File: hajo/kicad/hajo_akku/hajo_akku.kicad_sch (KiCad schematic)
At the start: 21 parts, among them J1 Seetalk NG, J2 Debug, J3 Batteries, U1 MCP2562, U2 LF50CV, U3 WeMos_S2_mini

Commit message: pcv rework
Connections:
- net DebugRX: now also J2.3 (Pin_3), U3.32 (GPIO40); no longer J2.4 (Pin_4), U3.15 (GPIO37)
- net DebugTX: now also J2.4 (Pin_4); no longer J2.3 (Pin_3)
- net GND: now also U1.8 (STBY), U3.17 (GPIO1); no longer U3.22 (GPIO10)
- net STBY: no longer names the net of U3.29 (GPIO34)
- net STBY: no longer U1.8 (STBY)
- no-connect marks 18 -> 21
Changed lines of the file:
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@@
   (junction (at 25.4 73.66) (diameter 0) (color 0 0 0 0)
   )
+  (junction (at 49.53 48.26) (diameter 0) (color 0 0 0 0)
+  )
   (junction (at 40.64 86.36) (diameter 0) (color 0 0 0 0)
   )
@@
   (junction (at 140.97 29.21) (diameter 0) (color 0 0 0 0)
   )
-  (no_connect (at 195.58 44.45))
   (no_connect (at 165.1 69.85))
   (no_connect (at 195.58 69.85))
   (no_connect (at 195.58 77.47))
+  (no_connect (at 165.1 64.77))
   (no_connect (at 195.58 52.07))
-  (no_connect (at 165.1 80.01))
+  (no_connect (at 165.1 72.39))
   (no_connect (at 165.1 54.61))
+  (no_connect (at 195.58 67.31))
   (no_connect (at 195.58 46.99))
   (no_connect (at 195.58 74.93))
@@
   (no_connect (at 165.1 39.37))
   (no_connect (at 195.58 62.23))
+  (no_connect (at 165.1 44.45))
+  (no_connect (at 165.1 46.99))
   (no_connect (at 195.58 57.15))
   (no_connect (at 195.58 64.77))
@@
     (stroke (width 0) (type default))
   )
-  (wire (pts (xy 49.53 46.99) (xy 49.53 49.53))
+  (wire (pts (xy 49.53 46.99) (xy 49.53 48.26))
     (stroke (width 0) (type default))
   )
@@
     (stroke (width 0) (type default))
   )
-  (wire (pts (xy 157.48 64.77) (xy 165.1 64.77))
-    (stroke (width 0) (type default))
-  )
   (wire (pts (xy 82.55 86.36) (xy 85.09 86.36))
     (stroke (width 0) (type default))
@@
     (stroke (width 0) (type default))
   )
+  (wire (pts (xy 49.53 48.26) (xy 49.53 50.8))
+    (stroke (width 0) (type default))
+  )
   (wire (pts (xy 154.94 77.47) (xy 165.1 77.47))
     (stroke (width 0) (type default))
@@
     (stroke (width 0) (type default))
   )
-  (wire (pts (xy 31.75 41.91) (xy 36.83 41.91))
+  (wire (pts (xy 34.29 48.26) (xy 49.53 48.26))
     (stroke (width 0) (type default))
   )
@@
     (stroke (width 0) (type default))
   )
-  (wire (pts (xy 154.94 72.39) (xy 165.1 72.39))
+  (wire (pts (xy 154.94 80.01) (xy 165.1 80.01))
     (stroke (width 0) (type default))
   )
@@
     (stroke (width 0) (type default))
   )
+  (wire (pts (xy 36.83 41.91) (xy 34.29 41.91))
+    (stroke (width 0) (type default))
+  )
   (wire (pts (xy 134.62 48.26) (xy 140.97 48.26))
     (stroke (width 0) (type default))
@@
     (stroke (width 0) (type default))
   )
+  (wire (pts (xy 195.58 44.45) (xy 203.2 44.45))
+    (stroke (width 0) (type default))
+  )
+  (wire (pts (xy 34.29 41.91) (xy 34.29 48.26))
+    (stroke (width 0) (type default))
+  )
   (wire (pts (xy 118.11 35.56) (xy 138.43 35.56))
     (stroke (width 0) (type default))
   )
-  (wire (pts (xy 203.2 67.31) (xy 203.2 68.58))
+  (wire (pts (xy 224.79 46.99) (xy 224.79 48.26))
     (stroke (width 0) (type default))
   )
@@
     (stroke (width 0) (type default))
   )
-  (wire (pts (xy 195.58 67.31) (xy 203.2 67.31))
-    (stroke (width 0) (type default))
-  )
   (wire (pts (xy 107.95 24.13) (xy 96.52 24.13))
     (stroke (width 0) (type default))
@@
     (effects (font (size 1.27 1.27)) (justify left bottom))
   )
-  (label "STBY" (at 31.75 41.91 0) (fields_autoplaced)
-    (effects (font (size 1.27 1.27)) (justify left bottom))
-  )
   (label "TXD" (at 157.48 59.69 0) (fields_autoplaced)
     (effects (font (size 1.27 1.27)) (justify left bottom))
   )
-  (label "DebugTX" (at 124.46 87.63 0) (fields_autoplaced)
+  (label "DebugTX" (at 124.46 85.09 0) (fields_autoplaced)
     (effects (font (size 1.27 1.27)) (justify left bottom))
   )
@@
     (effects (font (size 1.27 1.27)) (justify right bottom))
   )
-  (label "DebugRX" (at 124.46 85.09 0) (fields_autoplaced)
-    (effects (font (size 1.27 1.27)) (justify left bottom))
+  (label "DebugRX" (at 124.46 87.63 0) (fields_autoplaced)
+    (effects (font (size 1.27 1.27)) (justify left bottom))
+  )
+  (label "DevType" (at 203.2 44.45 180) (fields_autoplaced)
+    (effects (font (size 1.27 1.27)) (justify right bottom))
   )
   (label "ADC1" (at 138.43 19.05 180) (fields_autoplaced)
@@
     (effects (font (size 1.27 1.27)) (justify left bottom))
   )
-  (label "STBY" (at 157.48 64.77 0) (fields_autoplaced)
-    (effects (font (size 1.27 1.27)) (justify left bottom))
-  )
   (label "DebugTX" (at 154.94 77.47 0) (fields_autoplaced)
     (effects (font (size 1.27 1.27)) (justify left bottom))
   )
-  (label "DebugRX" (at 154.94 72.39 0) (fields_autoplaced)
+  (label "DebugRX" (at 154.94 80.01 0) (fields_autoplaced)
     (effects (font (size 1.27 1.27)) (justify left bottom))
   )
@@
   )
   (label "ADC3" (at 203.2 59.69 180) (fields_autoplaced)
+    (effects (font (size 1.27 1.27)) (justify right bottom))
+  )
+  (label "DevType" (at 224.79 46.99 180) (fields_autoplaced)
     (effects (font (size 1.27 1.27)) (justify right bottom))
   )
@@
     )
   )
-  (symbol (lib_id "power:GND") (at 49.53 49.53 0) (unit 1)
+  (symbol (lib_id "power:GND") (at 49.53 50.8 0) (unit 1)
     (in_bom yes) (on_board yes) (dnp no) (fields_autoplaced)
-    (property "Reference" "#PWR05" (at 49.53 55.88 0)
-      (effects (font (size 1.27 1.27)) hide)
-    )
-    (property "Value" "GND" (at 49.53 54.61 0)
-      (effects (font (size 1.27 1.27)))
-    )
-    (property "Footprint" "" (at 49.53 49.53 0)
-      (effects (font (size 1.27 1.27)) hide)
-    )
-    (property "Datasheet" "" (at 49.53 49.53 0)
+    (property "Reference" "#PWR05" (at 49.53 57.15 0)
+      (effects (font (size 1.27 1.27)) hide)
+    )
+    (property "Value" "GND" (at 49.53 55.88 0)
+      (effects (font (size 1.27 1.27)))
+    )
+    (property "Footprint" "" (at 49.53 50.8 0)
+      (effects (font (size 1.27 1.27)) hide)
+    )
+    (property "Datasheet" "" (at 49.53 50.8 0)
       (effects (font (size 1.27 1.27)) hide)
     )
@@
     )
   )
-  (symbol (lib_id "power:GND") (at 203.2 68.58 0) (unit 1)
+  (symbol (lib_id "power:GND") (at 224.79 48.26 0) (unit 1)
     (in_bom yes) (on_board yes) (dnp no) (fields_autoplaced)
-    (property "Reference" "#PWR012" (at 203.2 74.93 0)
-      (effects (font (size 1.27 1.27)) hide)
-    )
-    (property "Value" "GND" (at 203.2 73.66 0)
-      (effects (font (size 1.27 1.27)))
-    )
-    (property "Footprint" "" (at 203.2 68.58 0)
-      (effects (font (size 1.27 1.27)) hide)
-    )
-    (property "Datasheet" "" (at 203.2 68.58 0)
-      (effects (font (size 1.27 1.27)) hide)
-    )
+    (property "Reference" "#PWR012" (at 224.79 54.61 0)
+      (effects (font (size 1.27 1.27)) hide)
+    )
+    (property "Value" "GND" (at 224.79 53.34 0)
+      (effects (font (size 1.27 1.27)))
+    )
+    (property "Footprint" "" (at 224.79 48.26 0)
+      (effects (font (size 1.27 1.27)) hide)
+    )
+    (property "Datasheet" "" (at 224.79 48.26 0)
+      (effects (font (size 1.27 1.27)) hide)
+    )

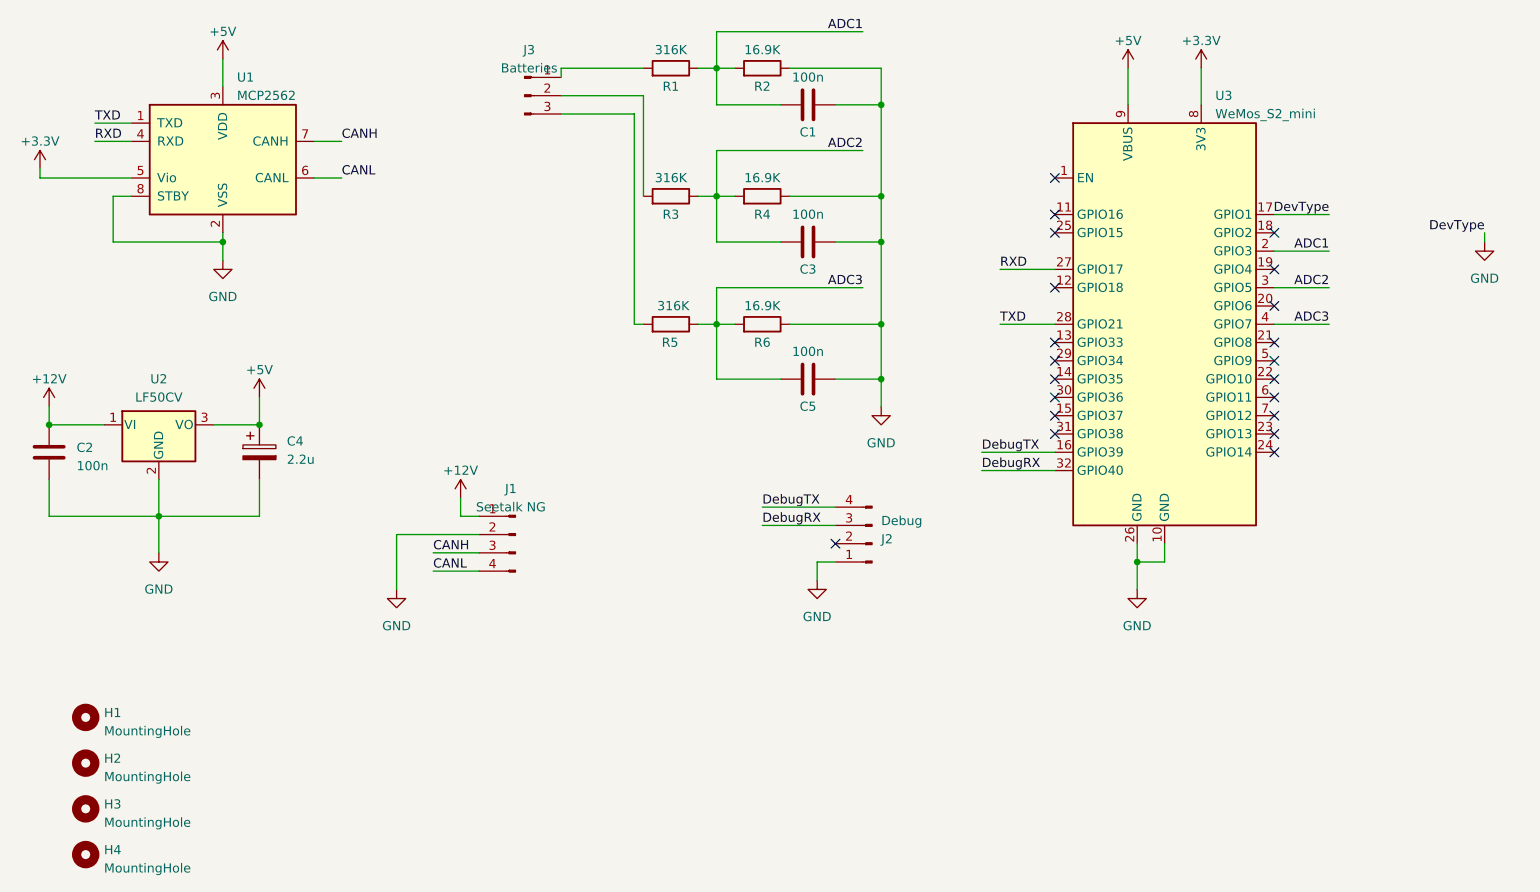
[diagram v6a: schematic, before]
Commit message: add back CanStby
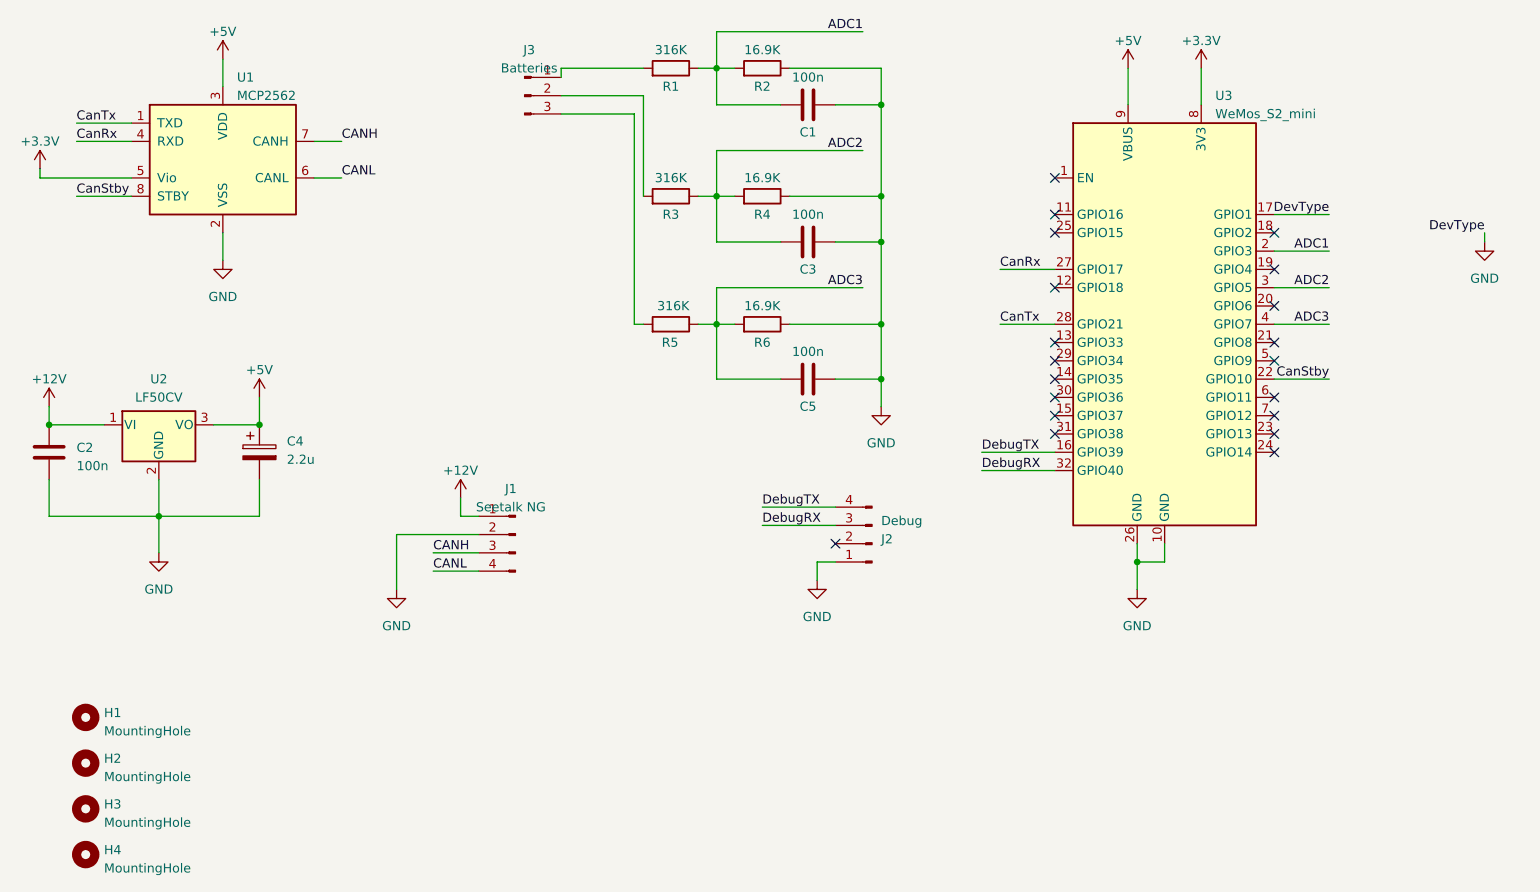
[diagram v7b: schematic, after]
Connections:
- net GND: no longer U1.8 (STBY)
- net CanStby: now reaches U3.22 (GPIO10)
- net CanStby: now also U1.8 (STBY)
- net RXD renamed CanRx
- net TXD renamed CanTx
- no-connect marks 21 -> 20
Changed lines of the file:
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@@
   (junction (at 25.4 73.66) (diameter 0) (color 0 0 0 0)
-  )
-  (junction (at 49.53 48.26) (diameter 0) (color 0 0 0 0)
   )
   (junction (at 40.64 86.36) (diameter 0) (color 0 0 0 0)
@@
   (no_connect (at 165.1 72.39))
   (no_connect (at 165.1 54.61))
-  (no_connect (at 195.58 67.31))
   (no_connect (at 195.58 46.99))
   (no_connect (at 195.58 74.93))
@@
     (stroke (width 0) (type default))
   )
-  (wire (pts (xy 49.53 46.99) (xy 49.53 48.26))
+  (wire (pts (xy 49.53 46.99) (xy 49.53 50.8))
     (stroke (width 0) (type default))
   )
@@
     (stroke (width 0) (type default))
   )
+  (wire (pts (xy 29.21 41.91) (xy 36.83 41.91))
+    (stroke (width 0) (type default))
+  )
   (wire (pts (xy 82.55 86.36) (xy 85.09 86.36))
     (stroke (width 0) (type default))
@@
     (stroke (width 0) (type default))
   )
-  (wire (pts (xy 49.53 48.26) (xy 49.53 50.8))
-    (stroke (width 0) (type default))
-  )
   (wire (pts (xy 154.94 77.47) (xy 165.1 77.47))
     (stroke (width 0) (type default))
@@
     (stroke (width 0) (type default))
   )
-  (wire (pts (xy 34.29 48.26) (xy 49.53 48.26))
-    (stroke (width 0) (type default))
-  )
   (wire (pts (xy 128.27 41.91) (xy 140.97 41.91))
     (stroke (width 0) (type default))
@@
     (stroke (width 0) (type default))
   )
+  (wire (pts (xy 195.58 67.31) (xy 203.2 67.31))
+    (stroke (width 0) (type default))
+  )
   (wire (pts (xy 25.4 86.36) (xy 40.64 86.36))
     (stroke (width 0) (type default))
   )
-  (wire (pts (xy 31.75 34.29) (xy 36.83 34.29))
+  (wire (pts (xy 29.21 34.29) (xy 36.83 34.29))
     (stroke (width 0) (type default))
   )
@@
     (stroke (width 0) (type default))
   )
-  (wire (pts (xy 36.83 41.91) (xy 34.29 41.91))
-    (stroke (width 0) (type default))
-  )
   (wire (pts (xy 134.62 48.26) (xy 140.97 48.26))
     (stroke (width 0) (type default))
@@
     (stroke (width 0) (type default))
   )
-  (wire (pts (xy 34.29 41.91) (xy 34.29 48.26))
-    (stroke (width 0) (type default))
-  )
   (wire (pts (xy 118.11 35.56) (xy 138.43 35.56))
     (stroke (width 0) (type default))
@@
     (stroke (width 0) (type default))
   )
-  (wire (pts (xy 31.75 31.75) (xy 36.83 31.75))
+  (wire (pts (xy 29.21 31.75) (xy 36.83 31.75))
     (stroke (width 0) (type default))
   )
@@
     (effects (font (size 1.27 1.27)) (justify left bottom))
   )
-  (label "TXD" (at 157.48 59.69 0) (fields_autoplaced)
+  (label "CanTx" (at 157.48 59.69 0) (fields_autoplaced)
     (effects (font (size 1.27 1.27)) (justify left bottom))
   )
@@
     (effects (font (size 1.27 1.27)) (justify right bottom))
   )
-  (label "RXD" (at 157.48 52.07 0) (fields_autoplaced)
+  (label "CanRx" (at 157.48 52.07 0) (fields_autoplaced)
     (effects (font (size 1.27 1.27)) (justify left bottom))
   )
@@
     (effects (font (size 1.27 1.27)) (justify right bottom))
   )
-  (label "RXD" (at 31.75 34.29 0) (fields_autoplaced)
-    (effects (font (size 1.27 1.27)) (justify left bottom))
-  )
-  (label "TXD" (at 31.75 31.75 0) (fields_autoplaced)
+  (label "CanRx" (at 29.21 34.29 0) (fields_autoplaced)
+    (effects (font (size 1.27 1.27)) (justify left bottom))
+  )
+  (label "CanTx" (at 29.21 31.75 0) (fields_autoplaced)
     (effects (font (size 1.27 1.27)) (justify left bottom))
   )
@@
     (effects (font (size 1.27 1.27)) (justify left bottom))
   )
+  (label "CanStby" (at 203.2 67.31 180) (fields_autoplaced)
+    (effects (font (size 1.27 1.27)) (justify right bottom))
+  )
   (label "DebugTX" (at 154.94 77.47 0) (fields_autoplaced)
     (effects (font (size 1.27 1.27)) (justify left bottom))
@@
     (effects (font (size 1.27 1.27)) (justify right bottom))
   )
+  (label "CanStby" (at 29.21 41.91 0) (fields_autoplaced)
+    (effects (font (size 1.27 1.27)) (justify left bottom))
+  )
   (label "CANL" (at 66.04 39.37 0) (fields_autoplaced)

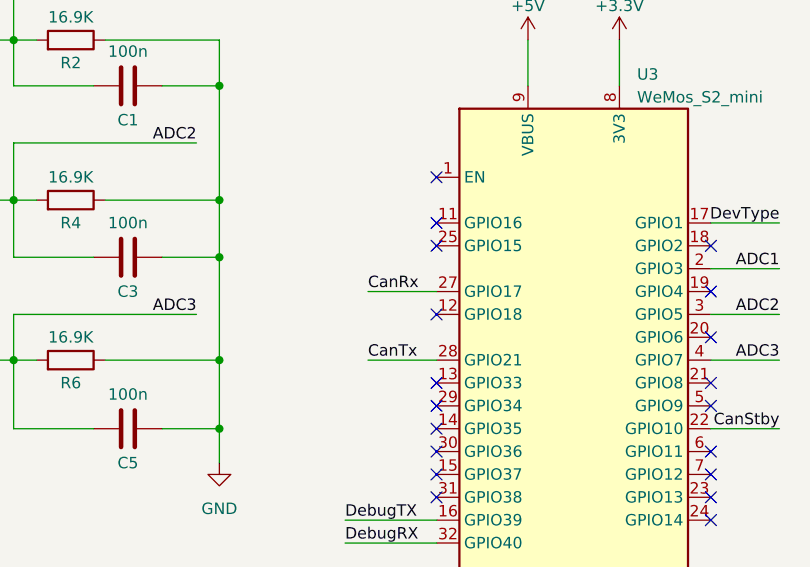
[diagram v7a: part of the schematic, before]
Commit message: fix mcp2562 pins
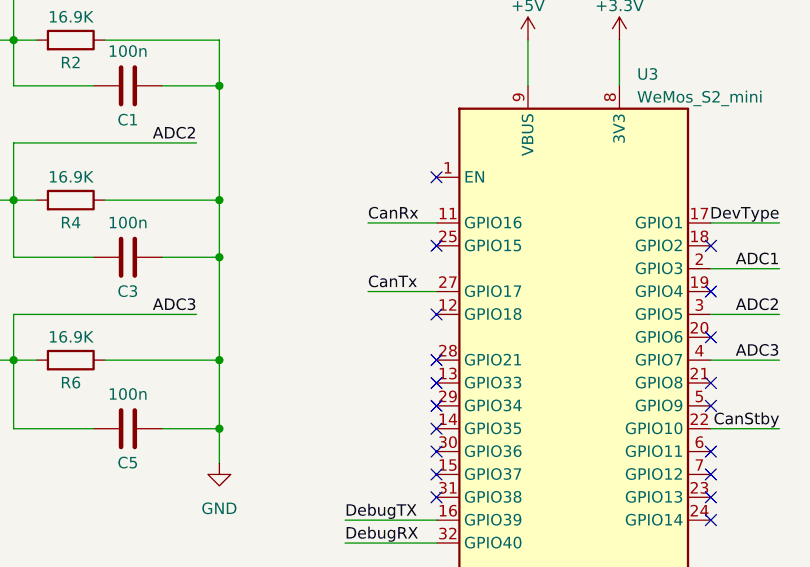
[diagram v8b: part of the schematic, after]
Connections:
- net CanRx: now also U3.11 (GPIO16); no longer U3.27 (GPIO17)
- net CanTx: now also U3.27 (GPIO17); no longer U3.28 (GPIO21)
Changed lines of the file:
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@@
   (no_connect (at 165.1 39.37))
   (no_connect (at 195.58 62.23))
-  (no_connect (at 165.1 44.45))
+  (no_connect (at 165.1 59.69))
   (no_connect (at 165.1 46.99))
   (no_connect (at 195.58 57.15))
@@
     (stroke (width 0) (type default))
   )
-  (wire (pts (xy 157.48 59.69) (xy 165.1 59.69))
+  (wire (pts (xy 157.48 44.45) (xy 165.1 44.45))
     (stroke (width 0) (type default))
   )
@@
     (effects (font (size 1.27 1.27)) (justify left bottom))
   )
-  (label "CanTx" (at 157.48 59.69 0) (fields_autoplaced)
+  (label "CanTx" (at 157.48 52.07 0) (fields_autoplaced)
     (effects (font (size 1.27 1.27)) (justify left bottom))
   )
@@
     (effects (font (size 1.27 1.27)) (justify right bottom))
   )
-  (label "CanRx" (at 157.48 52.07 0) (fields_autoplaced)
-    (effects (font (size 1.27 1.27)) (justify left bottom))
-  )
+  (label "CanRx" (at 157.48 44.45 0) (fields_autoplaced)
+    (effects (font (size 1.27 1.27)) (justify left bottom))
+  )
